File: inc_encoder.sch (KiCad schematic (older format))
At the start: 14 parts, among them U3 AM26LV32xD

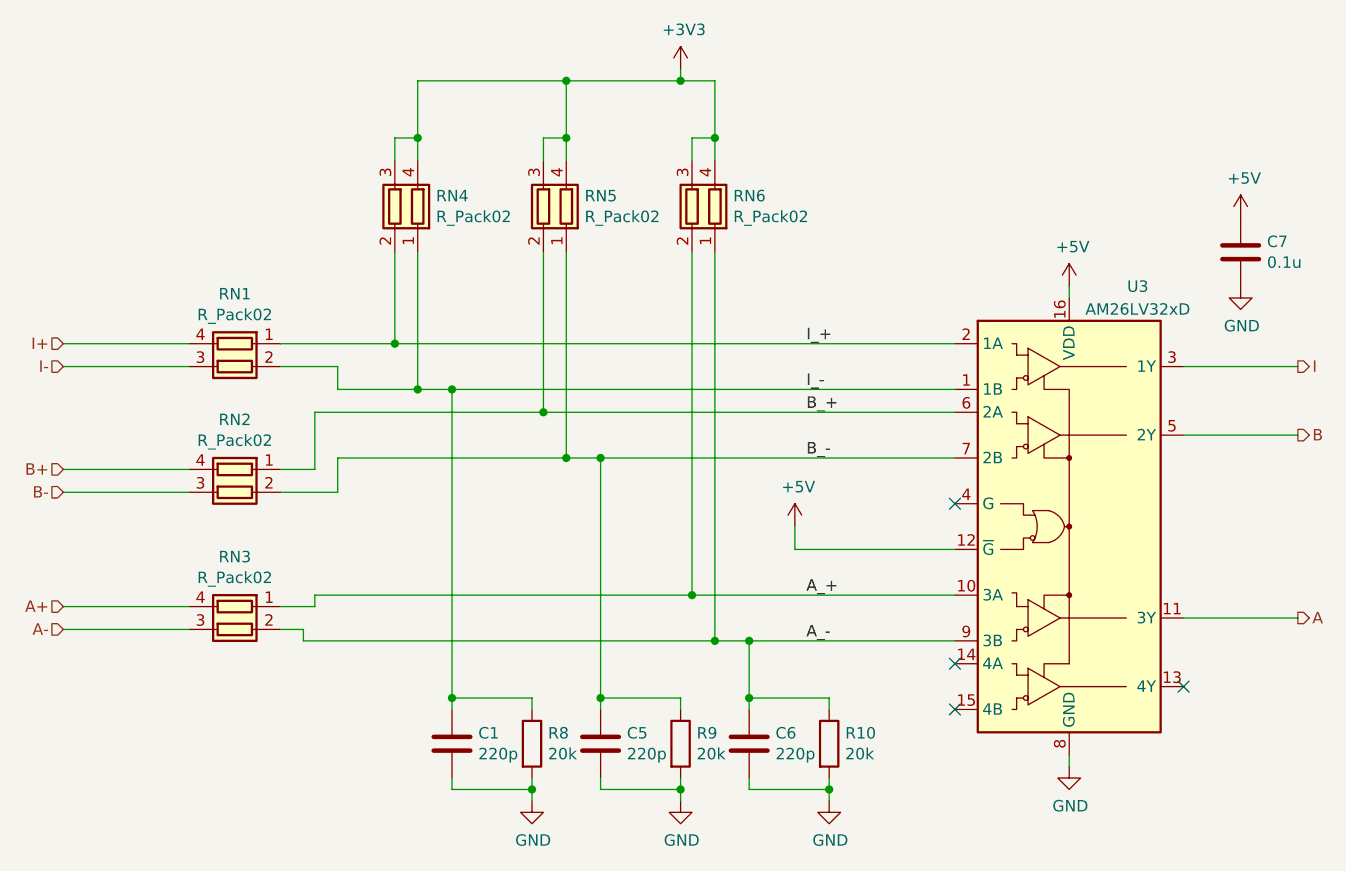
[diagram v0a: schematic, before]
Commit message: SPIにつなぐデバイスの電圧が違ったため設計ミスが判明。 これを修正した
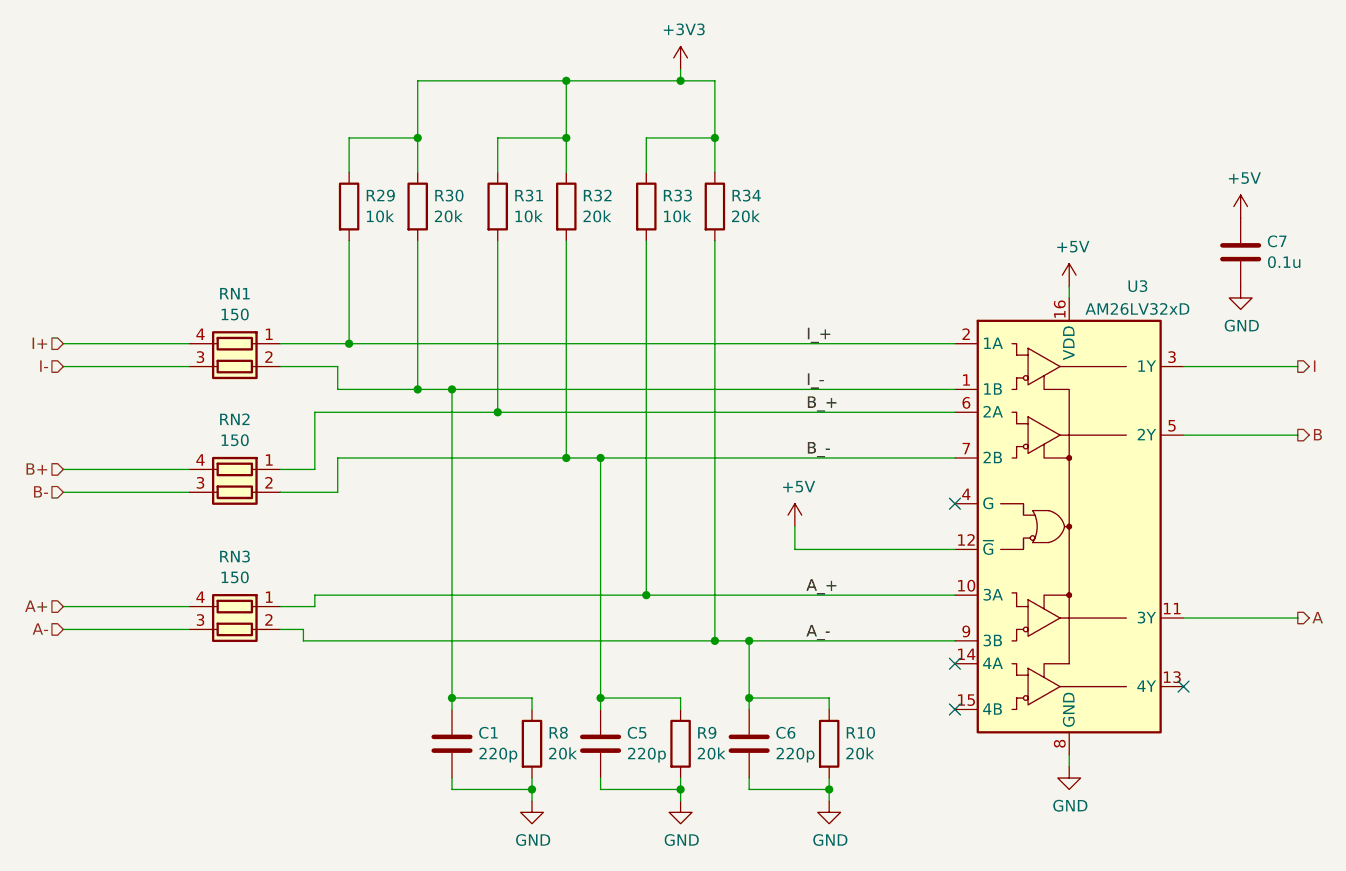
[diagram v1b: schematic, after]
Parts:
- removed RN4, RN5, RN6: R_Pack02, Resistor_SMD:R_Array_Concave_2x0603, symbol Device:R_Pack02
- added R29, R31, R33: 10k, Resistor_SMD:R_0603_1608Metric, symbol Device:R
- added R30, R32, R34: 20k, Resistor_SMD:R_0603_1608Metric, symbol Device:R
- RN1, RN2, RN3: value R_Pack02 -> 150
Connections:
- net +3V3: now also R29.1, R30.1, R31.1, R32.1, R33.1, R34.1
- net A_+: now also R33.2
- net A_-: now also R34.2
- net B_+: now also R31.2
- net B_-: now also R32.2
- net I_+: now also R29.2
- net I_-: now also R30.2
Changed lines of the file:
@@
 EESchema Schematic File Version 4
-LIBS:Encoder_check-cache
 EELAYER 30 0
 EELAYER END
@@
 	4850 2250 4850 2500
 Wire Wire Line
-	4750 2600 4750 2500
-Wire Wire Line
-	4750 2500 4850 2500
+	4550 2650 4550 2500
+Wire Wire Line
+	4550 2500 4850 2500
 Connection ~ 4850 2500
-Wire Wire Line
-	4850 2500 4850 2600
 Wire Wire Line
 	4700 2250 4200 2250
@@
 Connection ~ 4700 2250
 Wire Wire Line
-	4200 2500 4100 2500
+	4200 2500 3900 2500
 Connection ~ 4200 2500
 Wire Wire Line
-	4200 2500 4200 2600
-Wire Wire Line
-	4100 2600 4100 2500
+	3900 2650 3900 2500
 $Comp
 L Device:R R10
@@
 	4350 3900 5900 3900
 Wire Wire Line
-	2950 3400 3450 3400
+	2950 3400 3250 3400
 Wire Wire Line
 	3700 3600 3550 3600
 Wire Wire Line
-	3100 3700 4100 3700
-Wire Wire Line
-	3450 3000 3450 3400
-Connection ~ 3450 3400
-Wire Wire Line
-	3450 3400 5900 3400
-Wire Wire Line
-	3550 3000 3550 3600
+	3100 3700 3900 3700
+Wire Wire Line
+	3250 2950 3250 3400
+Connection ~ 3250 3400
+Wire Wire Line
+	3250 3400 5900 3400
+Wire Wire Line
+	3550 2950 3550 3600
 Connection ~ 3550 3600
 Wire Wire Line
-	4100 3000 4100 3700
-Connection ~ 4100 3700
-Wire Wire Line
-	4100 3700 5900 3700
-Wire Wire Line
-	4200 3000 4200 3900
+	3900 2950 3900 3700
+Connection ~ 3900 3700
+Wire Wire Line
+	3900 3700 5900 3700
 Connection ~ 4200 3900
 Wire Wire Line
@@
 Wire Wire Line
 	3100 4550 3100 4500
-$Comp
-L Device:R_Pack02 RN6
-U 1 1 5E4869DA
-P 4750 2800
-F 0 "RN6" H 4570 2846 50  0000 R CNN
-F 1 "R_Pack02" H 4570 2755 50  0000 R CNN
-F 2 "Resistor_SMD:R_Array_Concave_2x0603" V 4925 2800 50  0001 C CNN
-F 3 "~" H 4750 2800 50  0001 C CNN
-	1    4750 2800
-	-1   0    0    -1
-$EndComp
 $Comp
 L Device:R_Pack02 RN3
@@
 P 2750 4650
 F 0 "RN3" V 2433 4650 50  0000 C CNN
-F 1 "R_Pack02" V 2524 4650 50  0000 C CNN
+F 1 "150" V 2524 4650 50  0000 C CNN
 F 2 "Resistor_SMD:R_Array_Concave_2x0603" V 2925 4650 50  0001 C CNN
 F 3 "~" H 2750 4650 50  0001 C CNN
@@
 	0    -1   1    0
 $EndComp
-$Comp
-L Device:R_Pack02 RN5
-U 1 1 5E48D078
-P 4100 2800
-F 0 "RN5" H 3920 2846 50  0000 R CNN
-F 1 "R_Pack02" H 3920 2755 50  0000 R CNN
-F 2 "Resistor_SMD:R_Array_Concave_2x0603" V 4275 2800 50  0001 C CNN
-F 3 "~" H 4100 2800 50  0001 C CNN
-	1    4100 2800
-	-1   0    0    -1
-$EndComp
-$Comp
-L Device:R_Pack02 RN4
-U 1 1 5E48D4FD
-P 3450 2800
-F 0 "RN4" H 3270 2846 50  0000 R CNN
-F 1 "R_Pack02" H 3270 2755 50  0000 R CNN
-F 2 "Resistor_SMD:R_Array_Concave_2x0603" V 3625 2800 50  0001 C CNN
-F 3 "~" H 3450 2800 50  0001 C CNN
-	1    3450 2800
-	-1   0    0    -1
-$EndComp
-Wire Wire Line
-	3450 2600 3450 2500
-Wire Wire Line
-	3450 2500 3550 2500
-Wire Wire Line
-	3550 2500 3550 2600
+Wire Wire Line
+	3250 2650 3250 2500
+Wire Wire Line
+	3250 2500 3550 2500
+Wire Wire Line
+	3550 2500 3550 2650
 Wire Wire Line
 	3550 2500 3550 2250
@@
 P 2750 3500
 F 0 "RN1" V 2433 3500 50  0000 C CNN
-F 1 "R_Pack02" V 2524 3500 50  0000 C CNN
+F 1 "150" V 2524 3500 50  0000 C CNN
 F 2 "Resistor_SMD:R_Array_Concave_2x0603" V 2925 3500 50  0001 C CNN
 F 3 "~" H 2750 3500 50  0001 C CNN
@@
 P 2750 4050
 F 0 "RN2" V 2433 4050 50  0000 C CNN
-F 1 "R_Pack02" V 2524 4050 50  0000 C CNN
+F 1 "150" V 2524 4050 50  0000 C CNN
 F 2 "Resistor_SMD:R_Array_Concave_2x0603" V 2925 4050 50  0001 C CNN
 F 3 "~" H 2750 4050 50  0001 C CNN
@@
 	3050 4700 4850 4700
 Wire Wire Line
-	3100 4500 4750 4500
-Wire Wire Line
-	4750 3000 4750 4500
-Connection ~ 4750 4500
-Wire Wire Line
-	4750 4500 5900 4500
-Wire Wire Line
-	4850 3000 4850 4700
+	3100 4500 4550 4500
+Wire Wire Line
+	4550 2950 4550 4500
+Connection ~ 4550 4500
+Wire Wire Line
+	4550 4500 5900 4500
 Connection ~ 4850 4700
 Wire Wire Line
@@
 Text Label 5250 3400 0    50   ~ 0
 I_+
+$Comp
+L Device:R R34
+U 1 1 5E526854
+P 4850 2800
+F 0 "R34" H 4920 2846 50  0000 L CNN
+F 1 "20k" H 4920 2755 50  0000 L CNN
+F 2 "Resistor_SMD:R_0603_1608Metric" V 4780 2800 50  0001 C CNN
+F 3 "~" H 4850 2800 50  0001 C CNN
+	1    4850 2800
+	1    0    0    -1
+$EndComp
+$Comp
+L Device:R R32
+U 1 1 5E52703A
+P 4200 2800
+F 0 "R32" H 4270 2846 50  0000 L CNN
+F 1 "20k" H 4270 2755 50  0000 L CNN
+F 2 "Resistor_SMD:R_0603_1608Metric" V 4130 2800 50  0001 C CNN
+F 3 "~" H 4200 2800 50  0001 C CNN
+	1    4200 2800
+	1    0    0    -1
+$EndComp
+$Comp
+L Device:R R30
+U 1 1 5E5279AF
+P 3550 2800
+F 0 "R30" H 3620 2846 50  0000 L CNN
+F 1 "20k" H 3620 2755 50  0000 L CNN
+F 2 "Resistor_SMD:R_0603_1608Metric" V 3480 2800 50  0001 C CNN
+F 3 "~" H 3550 2800 50  0001 C CNN
+	1    3550 2800
+	1    0    0    -1
+$EndComp
+Wire Wire Line
+	4200 2500 4200 2650
+Wire Wire Line
+	4200 2950 4200 3900
+Wire Wire Line
+	4850 2950 4850 4700
+Wire Wire Line
+	4850 2500 4850 2650
+$Comp
+L Device:R R33
+U 1 1 5E531222
+P 4550 2800
+F 0 "R33" H 4620 2846 50  0000 L CNN
+F 1 "10k" H 4620 2755 50  0000 L CNN
+F 2 "Resistor_SMD:R_0603_1608Metric" V 4480 2800 50  0001 C CNN
+F 3 "~" H 4550 2800 50  0001 C CNN
+	1    4550 2800
+	1    0    0    -1
+$EndComp
+$Comp
+L Device:R R31
+U 1 1 5E539E90
+P 3900 2800
+F 0 "R31" H 3970 2846 50  0000 L CNN
+F 1 "10k" H 3970 2755 50  0000 L CNN
+F 2 "Resistor_SMD:R_0603_1608Metric" V 3830 2800 50  0001 C CNN
+F 3 "~" H 3900 2800 50  0001 C CNN
+	1    3900 2800
+	1    0    0    -1
+$EndComp
+$Comp
+L Device:R R29
+U 1 1 5E53A43F
+P 3250 2800
+F 0 "R29" H 3320 2846 50  0000 L CNN
+F 1 "10k" H 3320 2755 50  0000 L CNN
+F 2 "Resistor_SMD:R_0603_1608Metric" V 3180 2800 50  0001 C CNN
+F 3 "~" H 3250 2800 50  0001 C CNN
+	1    3250 2800
+	1    0    0    -1
+$EndComp
 $EndSCHEMATC
